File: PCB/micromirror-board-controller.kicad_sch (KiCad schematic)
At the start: 21 parts, among them J1 Barrel_Jack, J2 Conn_01x04_Female, J3 Conn_01x03_Female, J4 Conn_2Rows-51Pins, J5 USB_A, SW1 SW_Push, SW2 SW_Push, U1 Pico, U2 LM1117IMPX-5.0

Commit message: Clean up board silkscreen
Cleaned up silkscreen and added schematic pdf
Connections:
- net at R4.1: now also U1.32 (GPIO27_ADC1)
- net at U1.1 (GPIO0): now also SW1.2
- net at U1.14 (GPIO10): now also R3.1
- net at U1.2 (GPIO1): now also SW2.2
- no-connect marks 22 -> 21
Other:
- note added: "0.1.0"
- note added: "2023-03-25"
- note added: "Photon Ultra DLP controller board"
- moved on the sheet: C1, C2, C3, D1, D2, D3, D4, J2, J3, J5, JP1, R3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

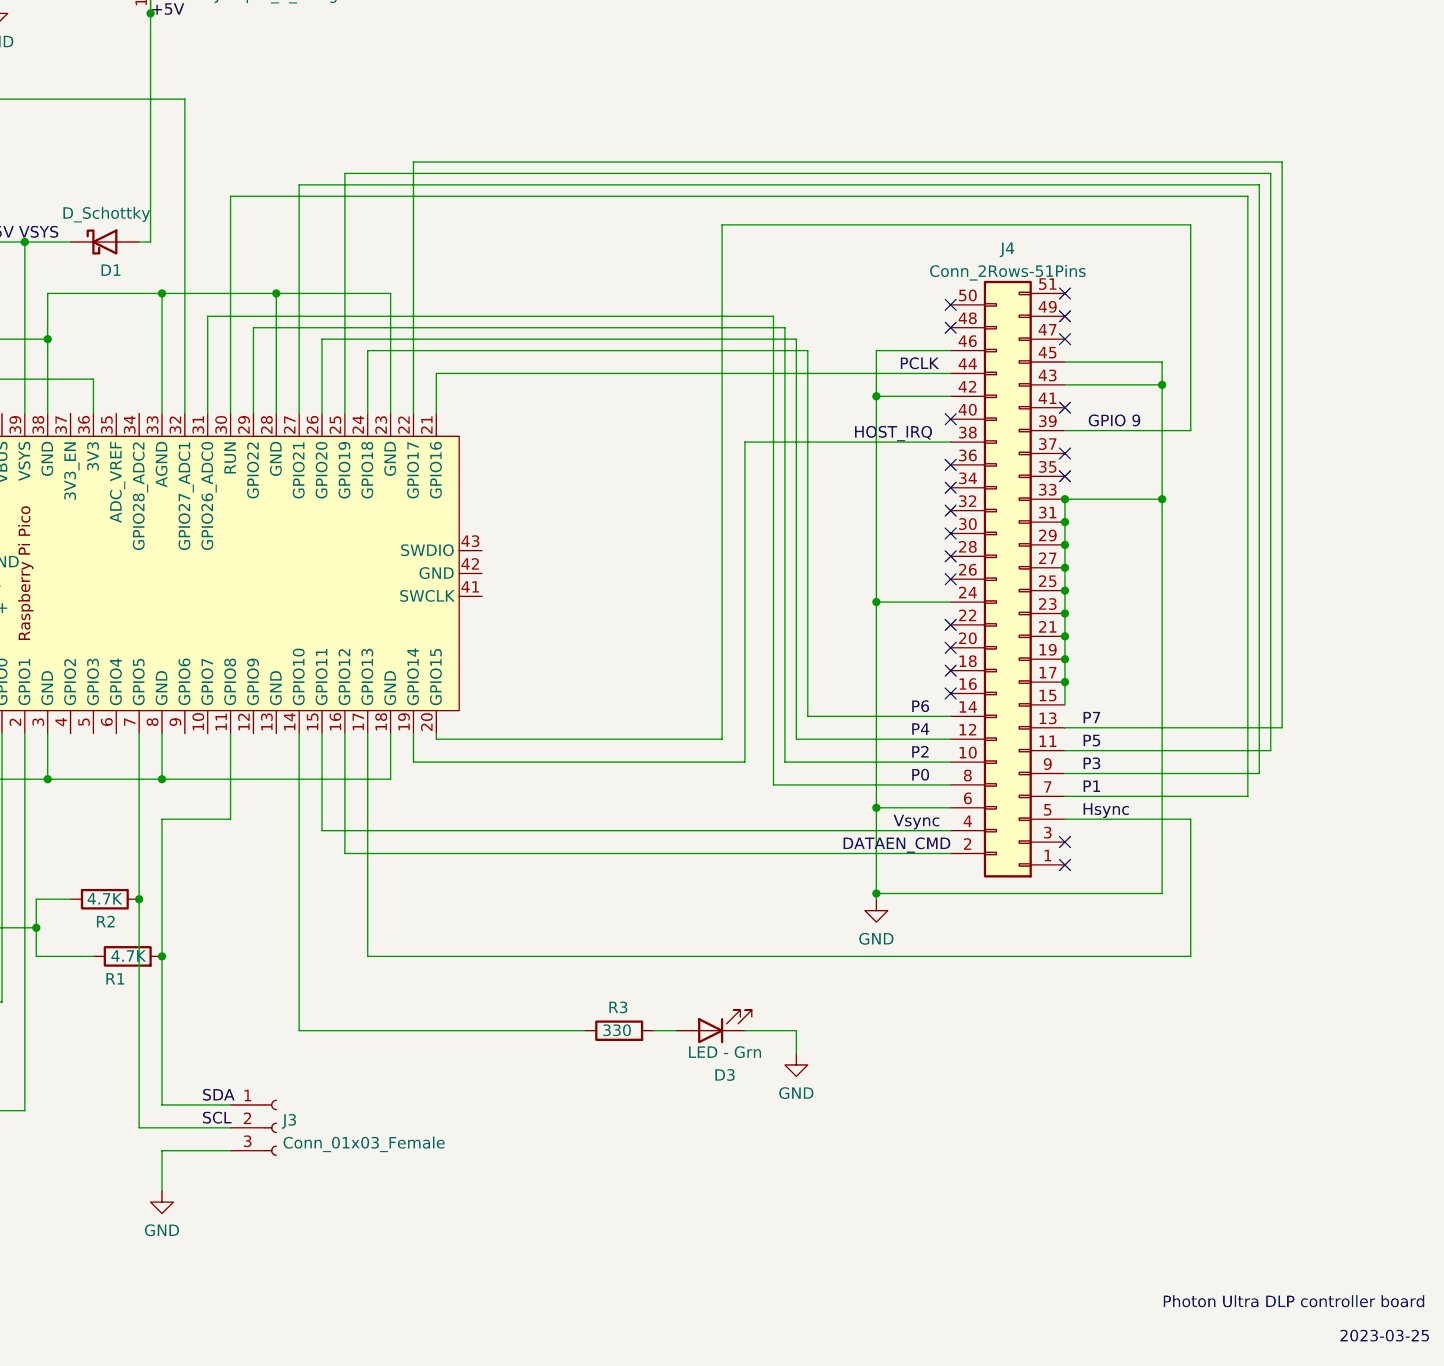
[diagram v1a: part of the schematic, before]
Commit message: Rearrangement of PCB traces and length matching
Needed to rearrange pins. Matched trace lengths; probably overkill.
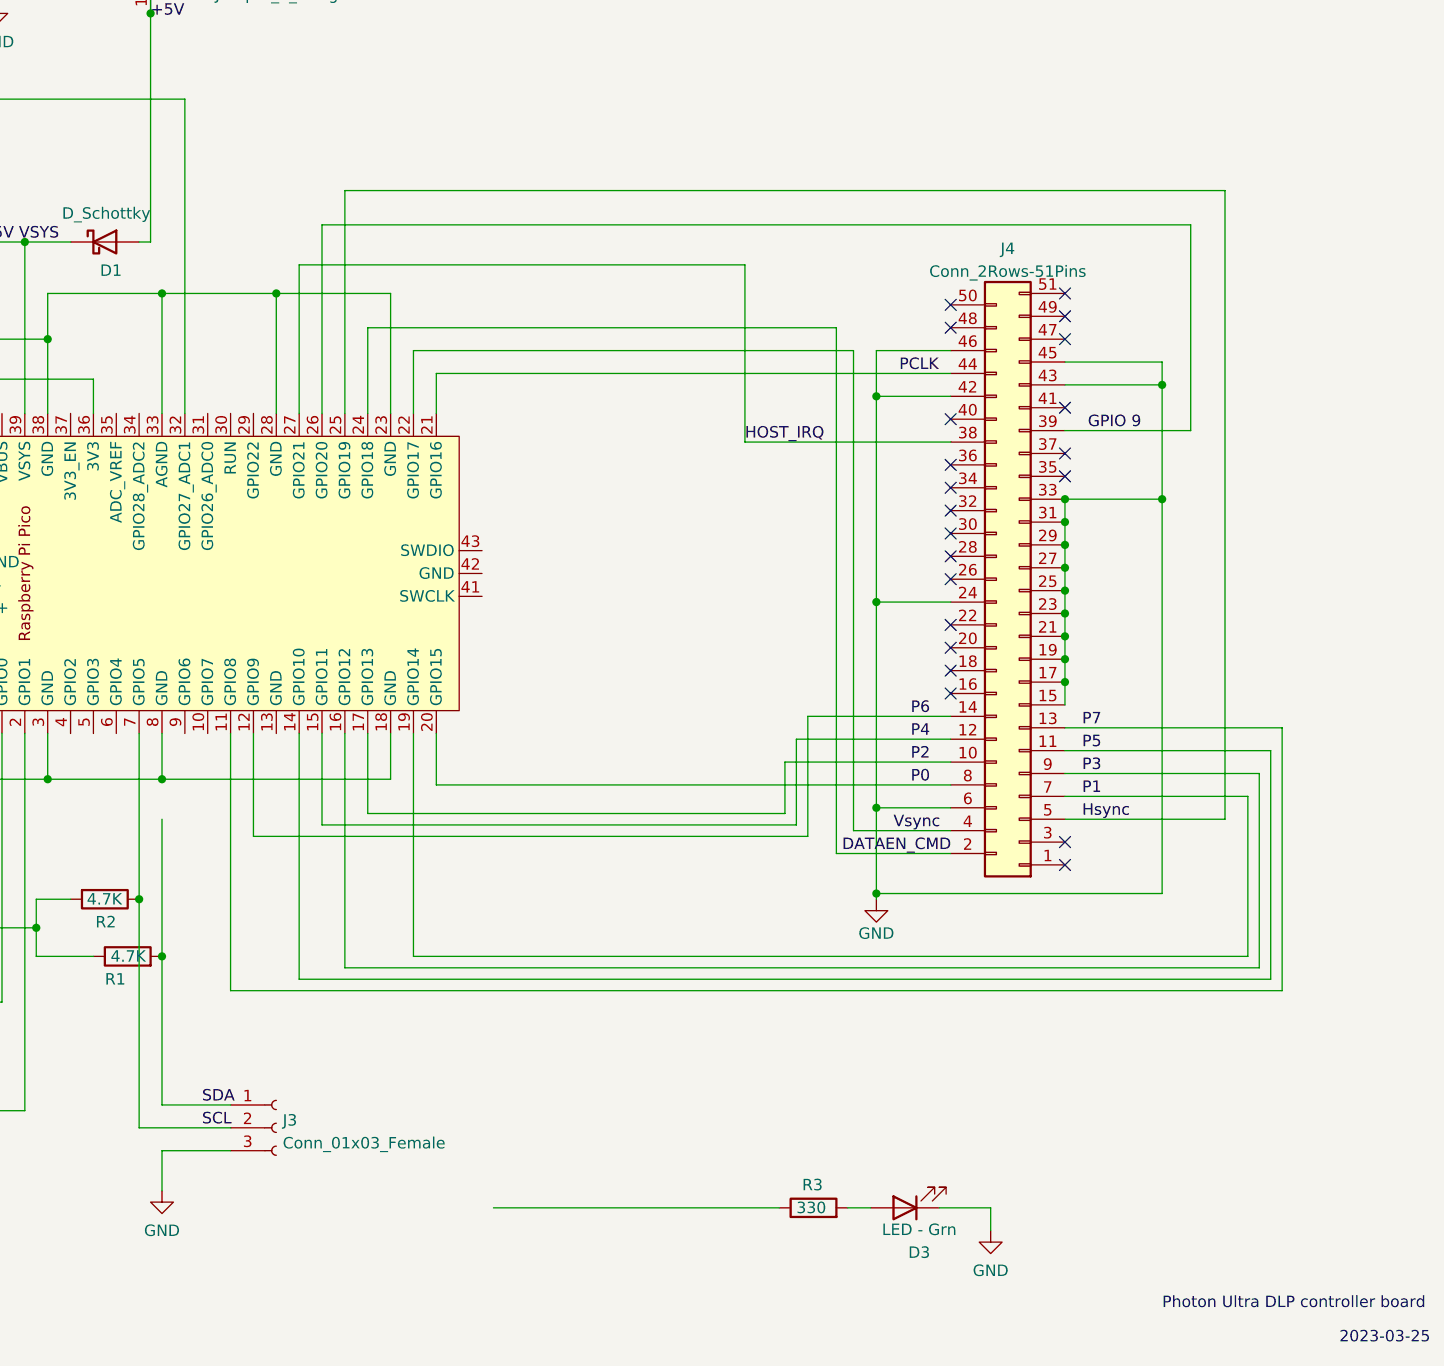
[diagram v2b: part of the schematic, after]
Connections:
- net DATAEN_CMD: now also U1.24 (GPIO18); no longer U1.16 (GPIO12)
- net GPIO 9: now also U1.26 (GPIO20); no longer U1.20 (GPIO15)
- net HOST_IRQ: now also U1.27 (GPIO21); no longer U1.19 (GPIO14)
- net Hsync: now also U1.25 (GPIO19); no longer U1.17 (GPIO13)
- net P0: now also U1.20 (GPIO15); no longer U1.31 (GPIO26_ADC0)
- net P1: now also U1.19 (GPIO14); no longer U1.30 (RUN)
- net P2: now also U1.17 (GPIO13); no longer U1.29 (GPIO22)
- net P3: now also U1.16 (GPIO12); no longer U1.27 (GPIO21)
- net P4: now also U1.15 (GPIO11); no longer U1.26 (GPIO20)
- net P5: now also U1.14 (GPIO10); no longer U1.25 (GPIO19)
- net P6: now also U1.12 (GPIO9); no longer U1.24 (GPIO18)
- net P7: now also U1.11 (GPIO8); no longer U1.22 (GPIO17)
- net SDA: no longer U1.11 (GPIO8)
- net Vsync: now also U1.22 (GPIO17); no longer U1.15 (GPIO11)
- net at R3.1: no longer U1.14 (GPIO10)
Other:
- moved on the sheet: D3, R3

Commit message: Finalised length-matched PCB
Fixed final few remaining traces with the new board layout.
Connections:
- net SCL: now also U1.10 (GPIO7); no longer U1.7 (GPIO5)
- net SDA: now also U1.9 (GPIO6)
- net at U1.32 (GPIO27_ADC1): no longer R4.1
- net LED green: now reaches U1.29 (GPIO22)
- net LED green: now also R3.1
- net LED red: now reaches U1.31 (GPIO26_ADC0)
- net LED red: now also R4.1
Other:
- note added: "0.1.1"
- note added: "2023-03-27"
- note removed: "0.1.0"
- note removed: "2023-03-25"
- moved on the sheet: D3, D4, J3, R1, R2, R3, R4

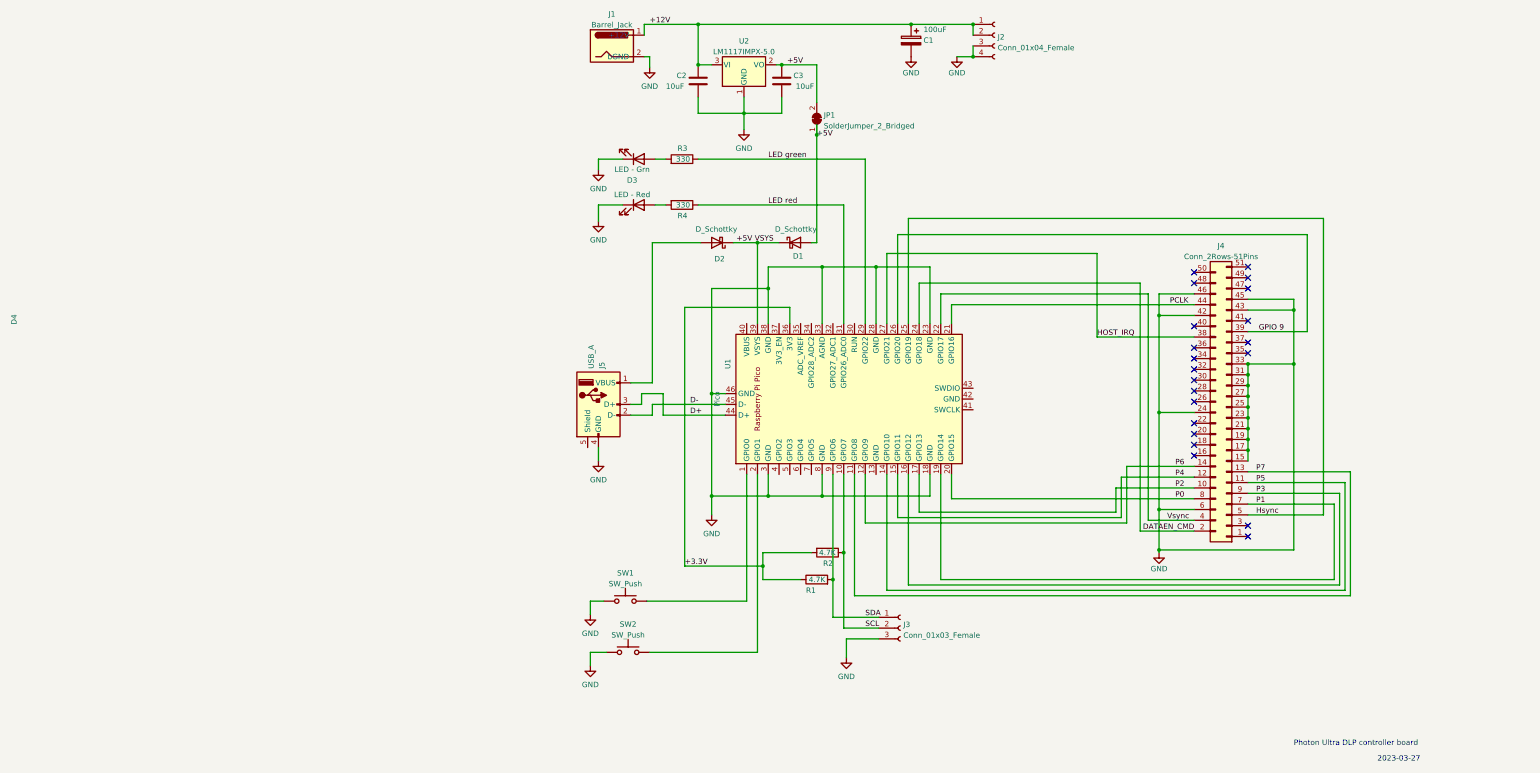
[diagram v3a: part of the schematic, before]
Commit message: Move to USB-C connector
Replacing the original type-A connector now a type-C connector. CC1/2 terminated with 5.1k.
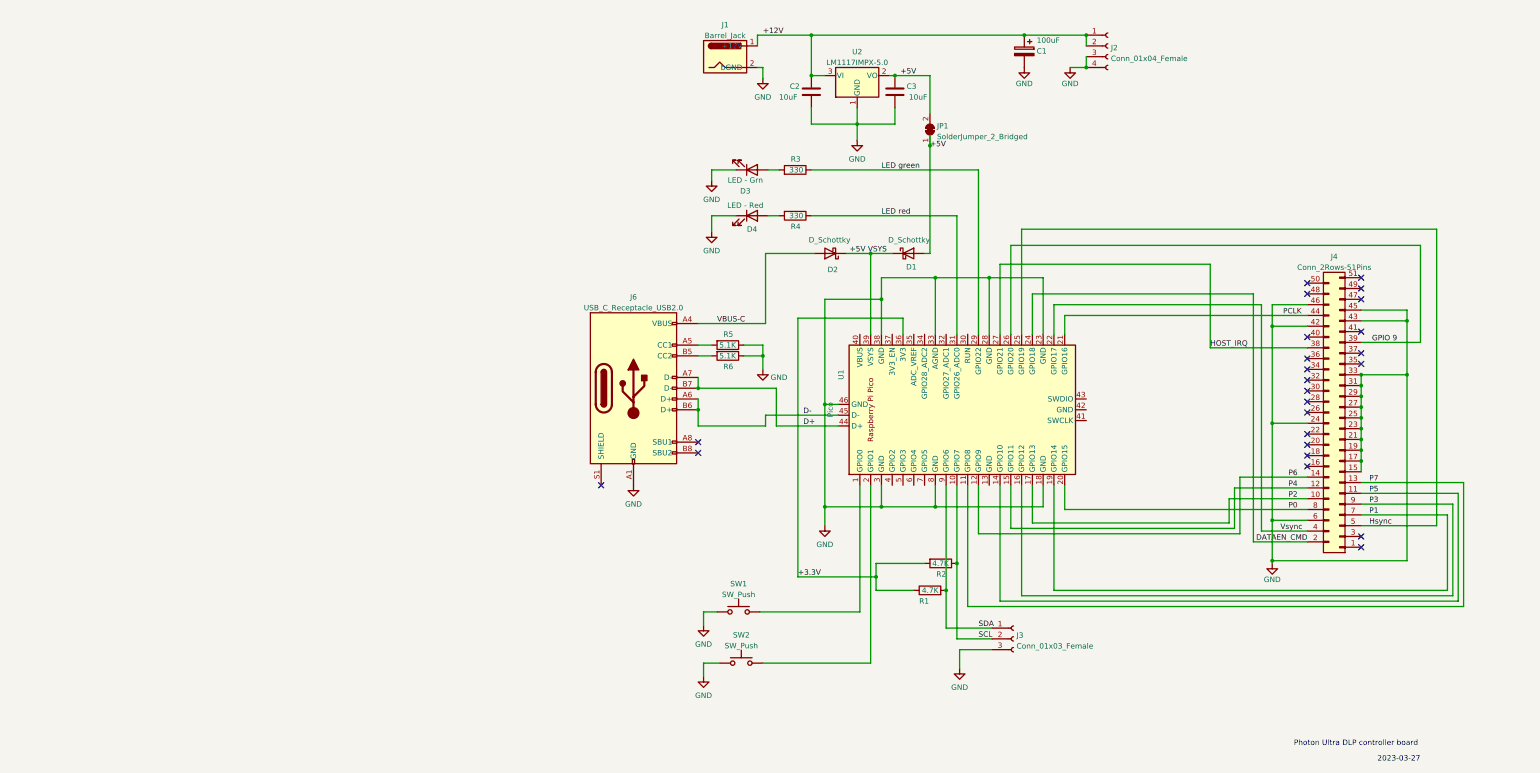
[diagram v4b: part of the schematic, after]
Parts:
- removed J5: USB_A, Connector_USB:USB_A_CONNFLY_DS1095-WNR0, symbol Connector:USB_A
- added J6: USB_C_Receptacle_USB2.0, Connector_USB:USB_C_Receptacle_HRO_TYPE-C-31-M-12, symbol Connector:USB_C_Receptacle_USB2.0
- added R5, R6: 5.1K, Resistor_SMD:R_1206_3216Metric, symbol Device:R
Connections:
- net D+: now also J6.A7 (D-), J6.B7 (D-)
- net D-: now also J6.A6 (D+), J6.B6 (D+)
- net GND: now also J6.A1 (GND), J6.A12 (GND), J6.B1 (GND), J6.B12 (GND), R5.1, R6.1
- net VBUS-C: now reaches D2.2 (A)
- net VBUS-C: now also J6.A4 (VBUS), J6.A9 (VBUS), J6.B4 (VBUS), J6.B9 (VBUS)
- new net: J6.A5 (CC1), R5.2
- new net: J6.B5 (CC2), R6.2
- no-connect marks 21 -> 24
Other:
- moved on the sheet: C1, C2, C3, D1, D2, D3, D4, J1, J2, J3, J4, JP1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
